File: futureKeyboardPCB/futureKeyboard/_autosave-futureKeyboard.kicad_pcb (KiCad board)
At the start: 2 copper layers, 118 parts, among them J1 Conn_01x01, J10 Conn_01x02, J11 Conn_01x01, J12 Conn_01x01, J13 Conn_01x04, J14 Conn_01x06, J15 Conn_01x06, J16 Conn_01x01, J17 Conn_01x15, J18 Conn_01x15, J19 Conn_01x15, J2 Conn_01x02, J20 Conn_01x15, J21 Conn_01x04, J22 Conn_01x04, J23 Conn_01x04, J24 Conn_01x04, J25 Conn_01x02, J3 Conn_01x01, J4 Conn_01x01, J5 Conn_01x04, J6 Conn_01x06, J7 Conn_01x06, J8 Conn_01x01, J9 Conn_01x01, P1 CONN_01X02, P2 CONN_01X06, P3 CONN_01X02, P4 CONN_01X06, Q1 2SC1815, Q2 2SC1815, Q3 2SC1815, Q4 2SC1815, Q5 2SC1815, Q6 2SC1815, SW1 SW_SPDT, SW10 SW_Push, SW11 SW_Push, SW12 SW_Push, SW13 SW_Push, SW14 SW_Push, SW15 SW_Push, SW16 SW_Push, SW17 SW_Push, SW18 SW_Push, SW19 SW_Push, SW2 SW_Push, SW20 SW_Push, SW21 SW_Push, SW22 SW_Push, SW23 SW_Push, SW24 SW_Push, SW25 SW_Push, SW3 SW_Push, SW4 SW_Push, SW5 SW_Push, SW6 SW_Push, SW7 SW_Push, SW8 SW_Push, SW9 SW_SPDT, U1 AMS1117-1.5, U2 ESP32, U3 AMS1117-1.5, U4 ESP32, U5 joystick

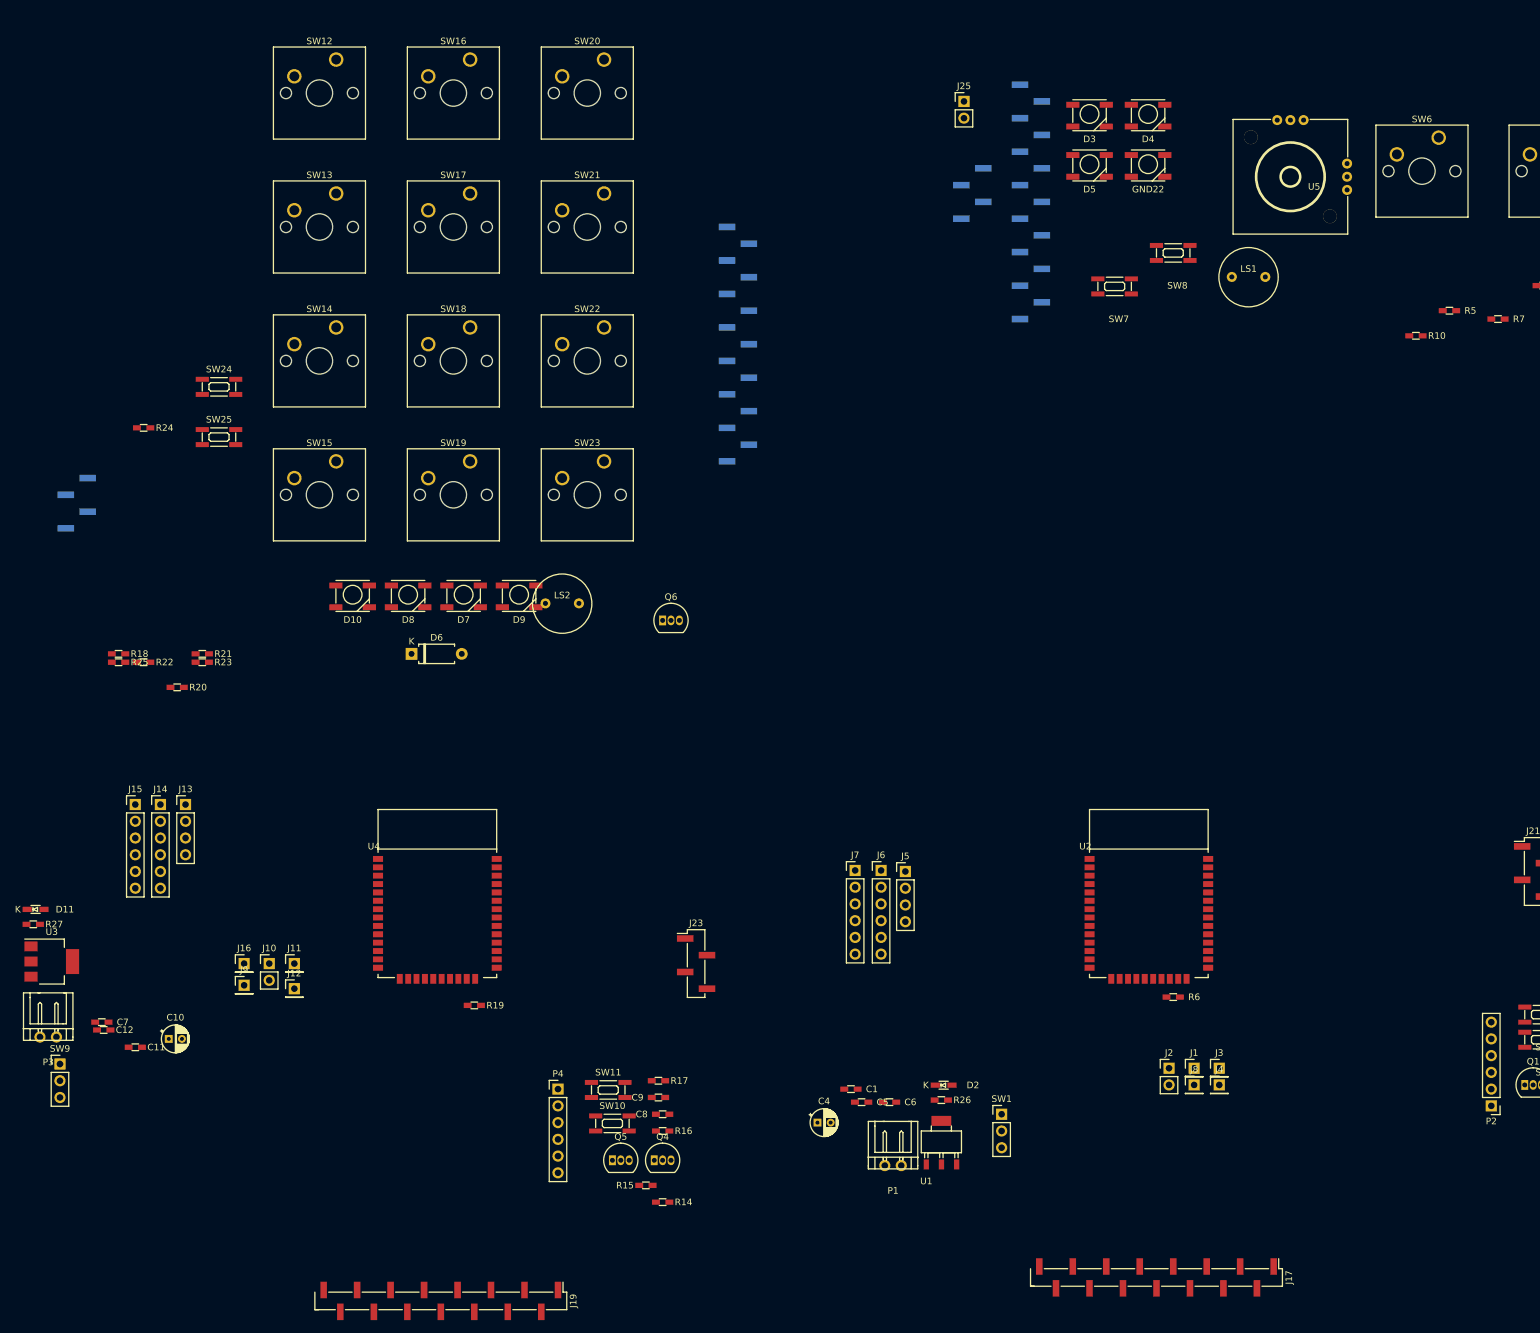
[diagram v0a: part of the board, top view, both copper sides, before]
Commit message: fix circuit bags, and placement electric parts
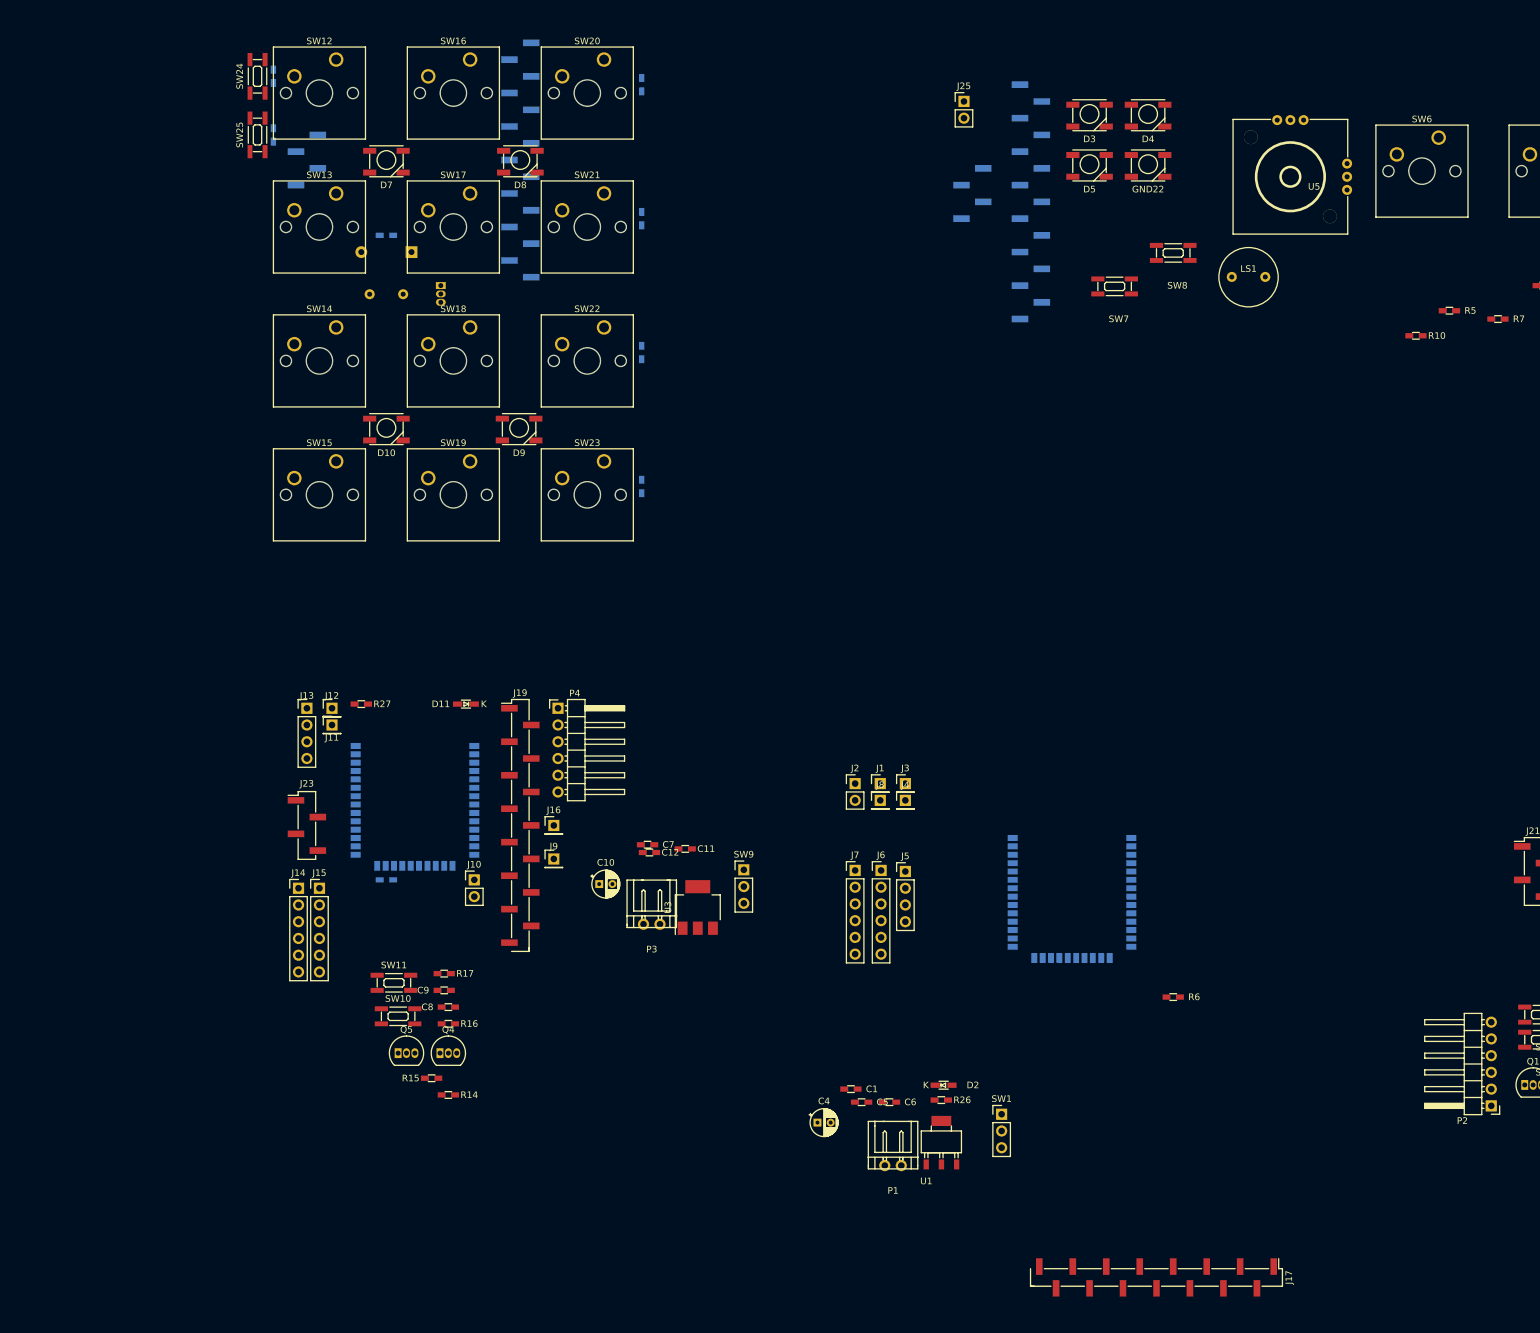
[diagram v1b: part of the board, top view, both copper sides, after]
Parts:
- D6, LS2, Q6, R18, R19, R20, R21, R22, R23, R24, R25, U2, U4: moved to B.Cu
- P2, P4: footprint Connector_PinHeader_2.54mm:PinHeader_1x06_P2.54mm_Vertical -> Connector_PinHeader_2.54mm:PinHeader_1x06_P2.54mm_Horizontal
- moved R20 115.5 mm to (109.9, 24.1), turned to 90 degrees
- moved SW9 107.9 mm to (125.3, 143.3)
- moved U3 98.4 mm to (118.4, 149.0), turned to 90 degrees
- moved R21 93.8 mm to (109.9, 44.5), turned to 90 degrees
- moved P3 93.2 mm to (111.4, 151.5)
- moved R22 89.0 mm to (109.9, 64.8), turned to 90 degrees
- moved C11 88.7 mm to (116.5, 140.1)
- moved C12 87.1 mm to (111.0, 140.6)
- moved C7 87.1 mm to (110.7, 139.4)
- moved R25 83.4 mm to (54.0, 31.8), turned to 270 degrees
- moved R18 75.4 mm to (71.1, 47.0), turned to 180 degrees
- moved J19 73.1 mm to (91.4, 136.5), turned to 0 degrees
- moved D11 72.3 mm to (83.2, 118.1), turned to 180 degrees
- moved R23 71.8 mm to (109.9, 85.1), turned to 90 degrees
- moved C10 69.4 mm to (103.4, 145.4)
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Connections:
- J17 pad 10: /Sheet5F548957/button1 -> /Sheet5F548957/dummy1
- J17 pad 11: /Sheet5F548957/button2 -> /Sheet5F548957/dummy2
- J17 pad 12: /Sheet5F548957/dummy1 -> /Sheet5F548957/button1
- J17 pad 13: /Sheet5F548957/dummy2 -> /Sheet5F548957/button2
- J17 pad 7: /Sheet5F548957/back -> /Sheet5F548957/enter
- J17 pad 9: /Sheet5F548957/enter -> /Sheet5F548957/back
- J18 pad 10: /Sheet5F548957/button12 -> /Sheet5F548957/dummy12
- J18 pad 11: /Sheet5F548957/button22 -> /Sheet5F548957/dummy22
- J18 pad 12: /Sheet5F548957/dummy12 -> /Sheet5F548957/button12
- J18 pad 13: /Sheet5F548957/dummy22 -> /Sheet5F548957/button22
